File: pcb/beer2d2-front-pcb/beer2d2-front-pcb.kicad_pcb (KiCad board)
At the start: 2 copper layers, 67.9 x 50.8 mm, 177 parts, among them IC1 ATMEGA168P, IC2 5VREG, IC3 TLC5971, J1 PSI_FRONT, J2 EYE_FRONT, J3 PSI_BACK, J4 RGB_EXTRA, J5 DCIN, M3 VAL**, P1 AVR_ISP, Q1 4403, Q10 4401, Q11 4401, Q12 4403, Q13 4401, Q14 4403, Q15 4401, Q2 4403, Q3 4401, Q4 4401, Q5 4403, Q6 4403, Q7 4401, Q8 4401, Q9 4403

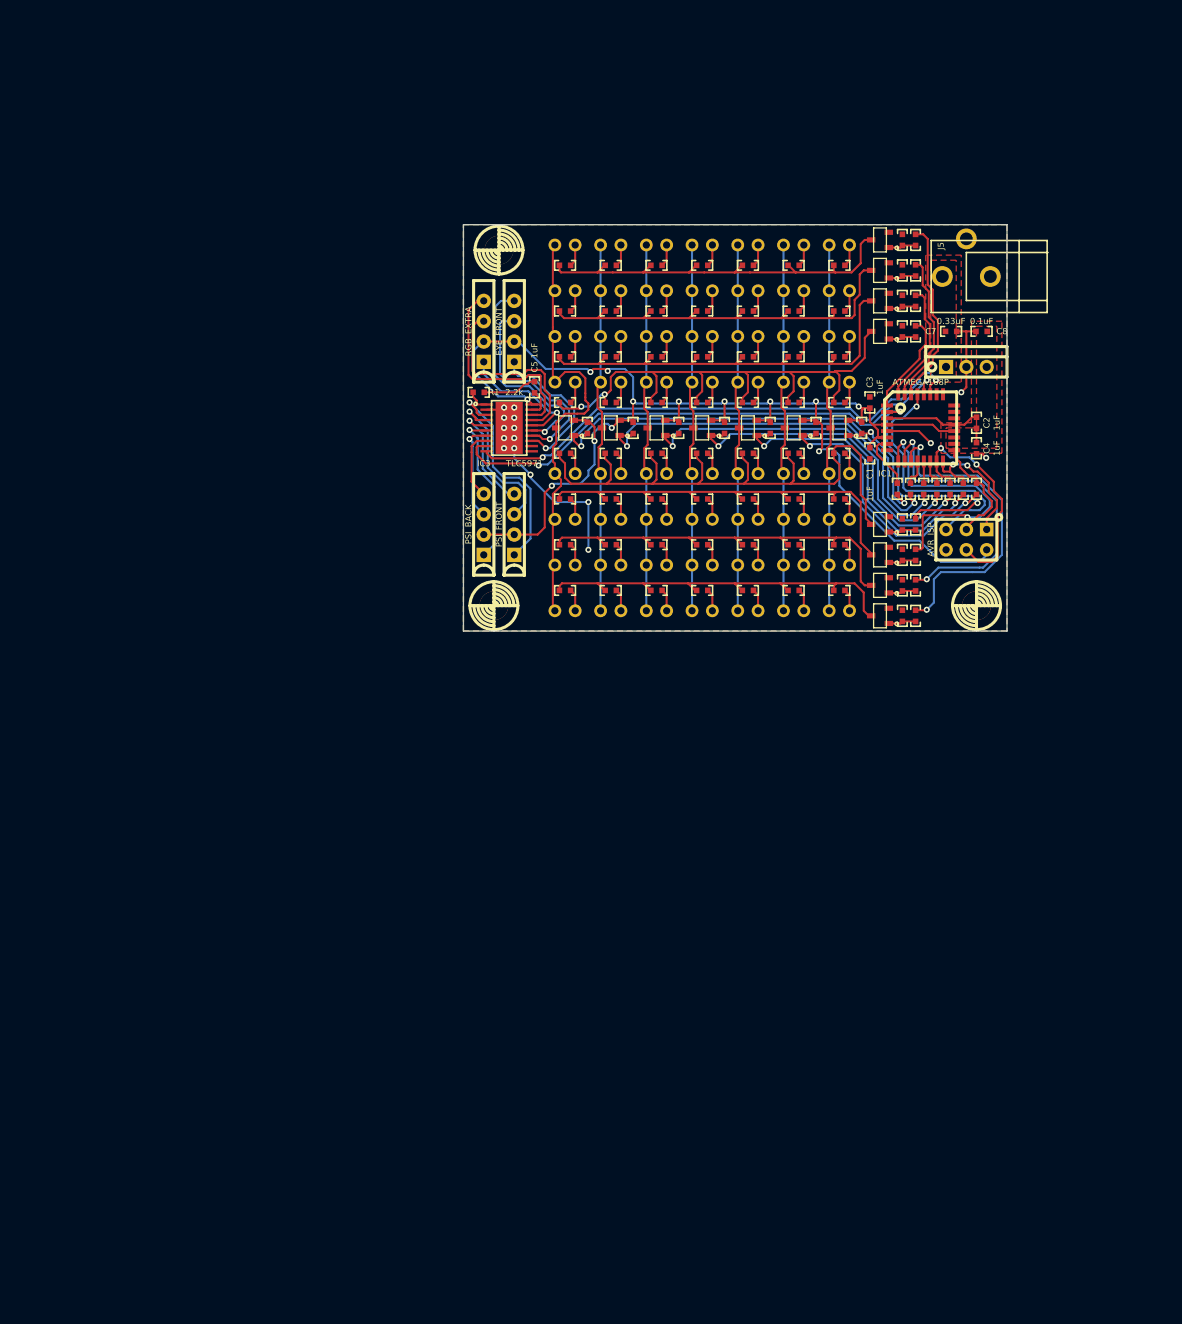
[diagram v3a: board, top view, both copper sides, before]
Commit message: redoing front board
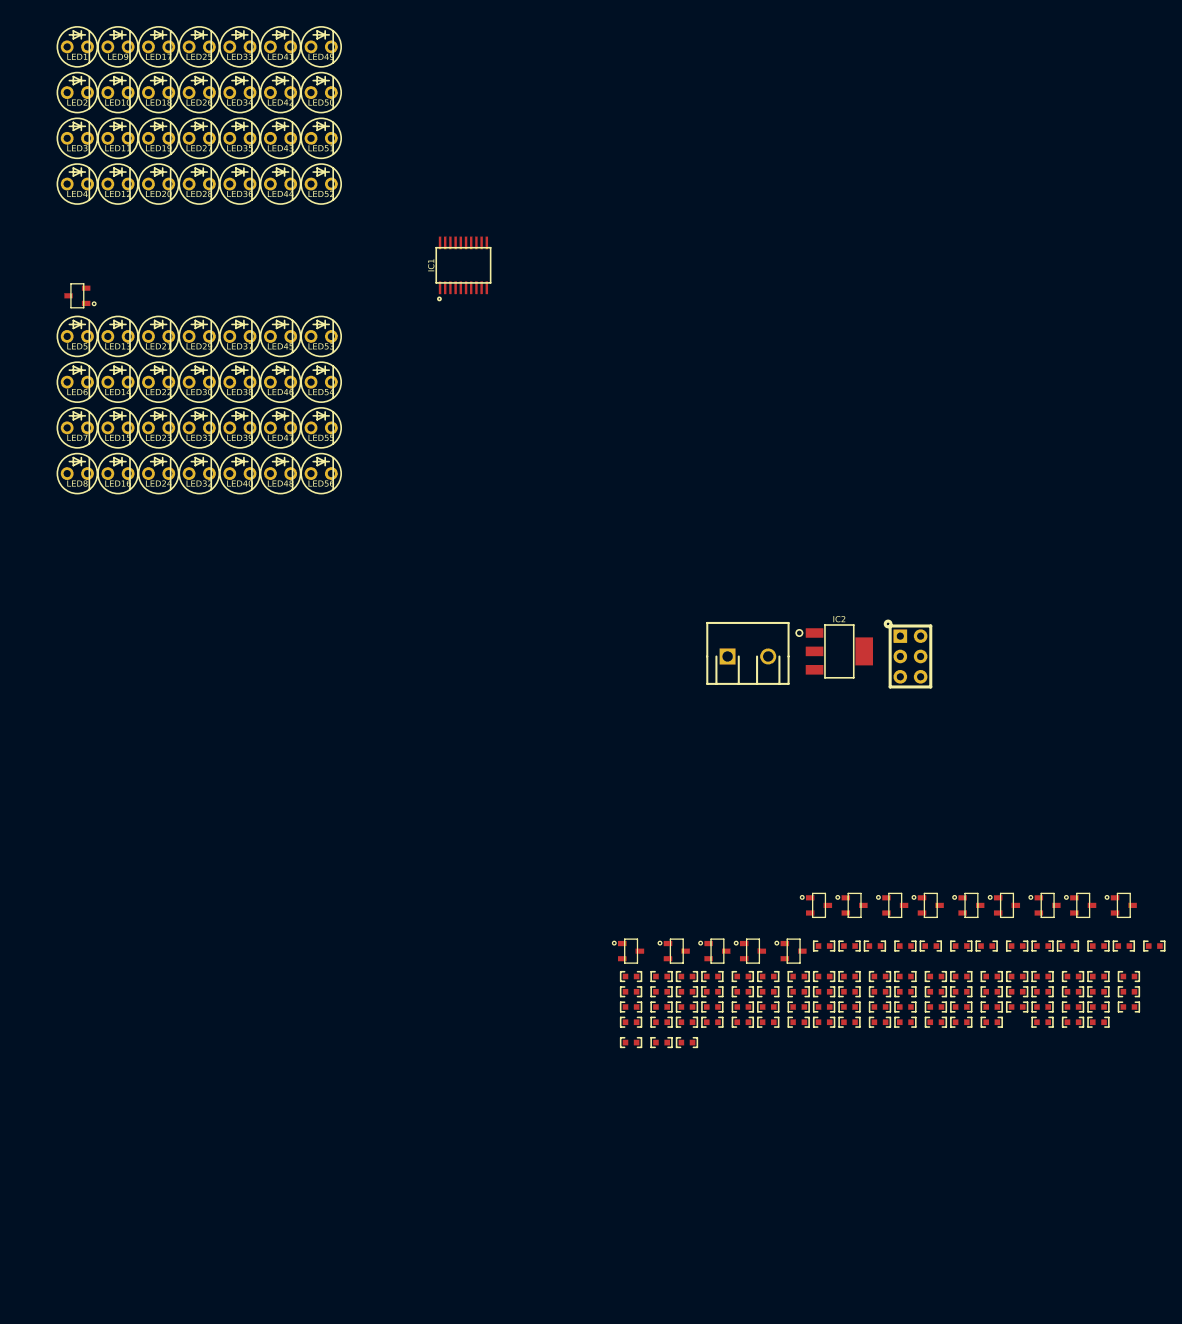
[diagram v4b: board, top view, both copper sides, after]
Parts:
- removed C3, C4: 1uF, 0603(1608m)
- removed C7: 0.1uF, 0603(1608m)
- removed C8: 0.33uF, 0603(1608m)
- removed IC3: TLC5971, HTSSOP20
- removed J2: EYE_FRONT, SIP4
- removed J3: PSI_BACK, SIP4
- removed J4: RGB_EXTRA, SIP4
- removed J5: DCIN, CUI_PJ-102A_DC-BARREL-JACK
- removed M3 (x3): VAL**, M3
- removed R87: 68Ω, 0603(1608m)
- added C6: 0.33uF, 0603(1608m), F.Cu at (233.7, 203.2)
- C1, C2, C5: value 1uF -> 0.1uF
- IC1: value ATMEGA168P -> ATTINY87/167_SO; footprint TQFP32_7mm -> TSSOP20
- IC2: value 5VREG -> LM1117; footprint TO220_3pin -> SOT223
- J1: value PSI_FRONT -> DCIN; footprint SIP4 -> 2-PIN_SCREW-TERM_P200MIL
- LED1, LED10, LED11, LED12, LED13, LED14, LED15, LED16, LED17, LED18, LED19, LED2, LED20, LED21, LED22, LED23, LED24, LED25, LED26, LED27, LED28, LED29, LED3, LED30, LED31, LED32, LED33, LED34, LED35, LED36, LED37, LED38, LED39, LED4, LED40, LED41, LED42, LED43, LED44, LED45, LED46, LED47, LED48, LED49, LED5, LED50, LED51, LED52, LED53, LED54, LED55, LED56, LED6, LED7, LED8, LED9: moved to F.Cu
- R1: value 2.2k -> 68Ω
- R11, R27, R42, R76: value 10kΩ -> 1kΩ
- R15, R31, R66, R78: value 1kΩ -> 10kΩ
- R17, R33, R56, R67, R79: value 10kΩ -> 68Ω
- R25, R41, R53, R75, R9: value 68Ω -> 10kΩ
- R45: value 1kΩ -> 68Ω
- R64: value 68Ω -> 1kΩ
- moved R18 102.5 mm to (261.0, 193.7), turned to 0 degrees
- moved R46 101.8 mm to (264.8, 197.5), turned to 0 degrees
- moved R16 97.1 mm to (264.8, 199.4), turned to 0 degrees
- moved R12 95.3 mm to (257.8, 199.4), turned to 0 degrees
- moved R32 95.1 mm to (210.2, 199.4), turned to 0 degrees
- moved R68 95.0 mm to (247.7, 201.3), turned to 0 degrees
- moved R80 94.8 mm to (237.5, 203.2), turned to 0 degrees
- moved R58 94.3 mm to (261.6, 199.4), turned to 0 degrees
- moved R19 94.2 mm to (254.6, 193.7), turned to 0 degrees
- moved R81 94.2 mm to (268.6, 201.3), turned to 0 degrees
- moved R57 93.2 mm to (230.5, 201.3), turned to 0 degrees
- moved R59 92.6 mm to (268.6, 199.4), turned to 0 degrees
- moved R3 91.6 mm to (243.8, 193.7), turned to 0 degrees
- moved R5 90.4 mm to (257.8, 193.7), turned to 0 degrees
- moved R28 90.2 mm to (244.5, 199.4), turned to 0 degrees
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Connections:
- C5 pad 1: GND -> N-000001
- C5 pad 2: VCC -> GND
- IC1 pad 1: /beer2d2 front LED panel/AVR_R3 -> /beer2d2 front LED panel/AVR_R0
- IC1 pad 10: /beer2d2 front LED panel/AVR_R6 -> /beer2d2 front LED panel/AVR_R7
- IC1 pad 11: /beer2d2 front LED panel/AVR_R7 -> /AVR_RST
- IC1 pad 12: /beer2d2 front LED panel/AVR_C0 -> /beer2d2 front LED panel/AVR_C6
- IC1 pad 13: /beer2d2 front LED panel/AVR_C1 -> /beer2d2 front LED panel/AVR_C5
- IC1 pad 14: /beer2d2 front LED panel/AVR_C2 -> /beer2d2 front LED panel/AVR_C4
- IC1 pad 15: /beer2d2 front LED panel/AVR_C3 -> VCC
- IC1 pad 16: /beer2d2 front LED panel/AVR_C4 -> GND
- IC1 pad 17: /beer2d2 front LED panel/AVR_C5 -> /beer2d2 front LED panel/AVR_C3
- IC1 pad 18: VCC -> /beer2d2 front LED panel/AVR_C2
- IC1 pad 19: (no net) -> /beer2d2 front LED panel/AVR_C1
- IC1 pad 2: /beer2d2 front LED panel/AVR_R4 -> /beer2d2 front LED panel/AVR_R1
- IC1 pad 20: VCC -> /beer2d2 front LED panel/AVR_C0
- IC1 pad 3: GND -> /beer2d2 front LED panel/AVR_R2
- IC1 pad 4: VCC -> /beer2d2 front LED panel/AVR_R3
- IC1 pad 5: GND -> VCC
- IC1 pad 6: VCC -> GND
- IC1 pad 7: /beer2d2 front LED panel/AVR_C6 -> /beer2d2 front LED panel/AVR_R4
- IC1 pad 8: (no net) -> /beer2d2 front LED panel/AVR_R5
- IC1 pad 9: /beer2d2 front LED panel/AVR_R5 -> /beer2d2 front LED panel/AVR_R6
- IC2 pad 1: /VIN -> GND
- IC2 pad 2: GND -> VCC
- IC2 pad 3: VCC -> N-000001
- J1 pad 1: /RED0 -> N-000001
- J1 pad 2: VCC -> GND
- LED1 pad 1: N-00000118 -> N-0000094
- LED10 pad 1: N-00000121 -> N-0000097
- LED11 pad 1: N-00000122 -> N-0000098
- LED12 pad 1: N-0000069 -> N-0000046
- LED13 pad 1: N-0000070 -> N-0000027
- LED14 pad 1: N-0000071 -> N-0000047
- LED15 pad 1: N-0000065 -> N-0000042
- LED16 pad 1: N-0000066 -> N-0000043
- LED17 pad 1: N-0000067 -> N-0000044
- LED18 pad 1: N-0000075 -> N-0000051
- LED19 pad 1: N-0000076 -> N-0000052
- LED2 pad 1: N-00000119 -> N-0000095
- LED20 pad 1: N-0000073 -> N-0000049
- LED21 pad 1: N-0000072 -> N-0000048
- LED22 pad 1: N-0000074 -> N-0000050
- LED23 pad 1: N-0000051 -> N-0000028
- LED24 pad 1: N-0000052 -> N-0000029
- LED25 pad 1: N-0000054 -> N-0000031
- LED26 pad 1: N-0000046 -> N-0000022
- LED27 pad 1: N-0000044 -> N-0000020
- LED28 pad 1: N-0000048 -> N-0000024
- LED29 pad 1: N-0000059 -> N-0000036
- LED3 pad 1: N-00000114 -> N-0000090
- LED30 pad 1: N-0000062 -> N-0000039
- LED31 pad 1: N-0000064 -> N-0000041
- LED32 pad 1: N-0000056 -> N-0000033
- LED33 pad 1: N-0000057 -> N-0000034
- LED34 pad 1: N-0000058 -> N-0000035
- LED35 pad 1: N-0000094 -> N-0000070
- LED36 pad 1: N-0000095 -> N-0000071
- LED37 pad 1: N-0000090 -> N-0000066
- LED38 pad 1: N-0000091 -> N-0000067
- LED39 pad 1: N-0000092 -> N-0000068
- LED4 pad 1: N-00000115 -> N-0000091
- LED40 pad 1: N-0000093 -> N-0000069
- LED41 pad 1: N-0000099 -> N-0000075
- LED42 pad 1: N-00000100 -> N-0000076
- LED43 pad 1: N-0000097 -> N-0000073
- LED44 pad 1: N-0000098 -> N-0000074
- LED45 pad 1: N-0000087 -> N-0000063
- LED46 pad 1: N-0000080 -> N-0000056
- LED47 pad 1: N-0000081 -> N-0000057
- LED48 pad 1: N-0000082 -> N-0000058
- LED49 pad 1: N-0000077 -> N-0000053
- LED5 pad 1: N-00000116 -> N-0000092
- LED50 pad 1: N-0000078 -> N-0000054
- LED51 pad 1: N-0000079 -> N-0000055
- LED52 pad 1: N-0000086 -> N-0000062
- LED53 pad 1: N-0000088 -> N-0000064
- LED54 pad 1: N-0000084 -> N-0000060
- LED55 pad 1: N-0000083 -> N-0000059
- LED56 pad 1: N-0000085 -> N-0000061
- LED6 pad 1: N-00000117 -> N-0000093
- LED7 pad 1: N-00000123 -> N-0000099
- LED8 pad 1: N-00000124 -> N-00000100
- LED9 pad 1: N-00000120 -> N-0000096
- P1 pad 1: /beer2d2 front LED panel/AVR_C4 -> /beer2d2 front LED panel/AVR_R2
- P1 pad 3: /beer2d2 front LED panel/AVR_C5 -> /beer2d2 front LED panel/AVR_R5
- P1 pad 4: /beer2d2 front LED panel/AVR_C3 -> /beer2d2 front LED panel/AVR_R4
- Q1 pad 1: N-00000109 -> N-0000085
- Q10 pad 1: N-00000113 -> N-0000089
- Q11 pad 1: N-00000106 -> N-0000082
- Q12 pad 1: N-00000125 -> N-00000101
- Q13 pad 1: N-00000110 -> N-0000086
- Q14 pad 1: N-00000129 -> N-00000105
- Q15 pad 1: N-00000103 -> N-0000079
- Q2 pad 1: N-00000127 -> N-00000103
- Q3 pad 1: N-00000107 -> N-0000083
- Q4 pad 1: N-00000102 -> N-0000078
- Q5 pad 1: N-00000104 -> N-0000080
- Q6 pad 1: N-00000128 -> N-00000104
- Q7 pad 1: N-00000111 -> N-0000087
- Q8 pad 1: N-00000105 -> N-0000081
- Q9 pad 1: N-00000126 -> N-00000102
- R1 pad 1: GND -> N-0000094
- R1 pad 2: N-0000038 -> /beer2d2 front LED panel/ROW0
- R10 pad 2: N-00000109 -> N-00000103
- R11 pad 1: VCC -> /beer2d2 front LED panel/AVR_R0
- R11 pad 2: N-00000127 -> N-0000083
- R12 pad 1: /beer2d2 front LED panel/AVR_R0 -> /beer2d2 front LED panel/AVR_R5
- R12 pad 2: N-00000107 -> N-0000078
- R13 pad 1: /beer2d2 front LED panel/AVR_R5 -> N-0000085
- R13 pad 2: N-00000102 -> /beer2d2 front LED panel/AVR_C0
- R14 pad 1: N-00000109 -> N-00000103
- R14 pad 2: /beer2d2 front LED panel/AVR_C0 -> /beer2d2 front LED panel/AVR_C5
- R15 pad 1: N-00000127 -> N-0000083
- R15 pad 2: /beer2d2 front LED panel/AVR_C5 -> GND
- R16 pad 1: N-00000107 -> N-0000078
- R17 pad 1: N-00000102 -> N-0000096
- R17 pad 2: GND -> /beer2d2 front LED panel/ROW0
- R18 pad 1: N-00000120 -> N-0000097
- R18 pad 2: /beer2d2 front LED panel/ROW0 -> /beer2d2 front LED panel/ROW1
- R19 pad 1: N-00000121 -> N-0000098
- R19 pad 2: /beer2d2 front LED panel/ROW1 -> /beer2d2 front LED panel/ROW2
- R2 pad 1: N-00000118 -> N-0000095
- R2 pad 2: /beer2d2 front LED panel/ROW0 -> /beer2d2 front LED panel/ROW1
- R20 pad 1: N-00000122 -> N-0000046
- R20 pad 2: /beer2d2 front LED panel/ROW2 -> /beer2d2 front LED panel/ROW3
- R21 pad 1: N-0000069 -> N-0000027
- R21 pad 2: /beer2d2 front LED panel/ROW3 -> /beer2d2 front LED panel/ROW4
- R22 pad 1: N-0000070 -> N-0000047
- R22 pad 2: /beer2d2 front LED panel/ROW4 -> /beer2d2 front LED panel/ROW5
- R23 pad 1: N-0000071 -> N-0000042
- R23 pad 2: /beer2d2 front LED panel/ROW5 -> /beer2d2 front LED panel/ROW6
- R24 pad 1: N-0000065 -> N-0000043
- R24 pad 2: /beer2d2 front LED panel/ROW6 -> /beer2d2 front LED panel/ROW7
- R25 pad 1: N-0000066 -> VCC
- R25 pad 2: /beer2d2 front LED panel/ROW7 -> N-0000080
- R27 pad 1: VCC -> /beer2d2 front LED panel/AVR_R1
- R27 pad 2: N-00000128 -> N-0000087
- R28 pad 1: /beer2d2 front LED panel/AVR_R1 -> /beer2d2 front LED panel/AVR_R6
- R28 pad 2: N-00000111 -> N-0000081
- R29 pad 1: /beer2d2 front LED panel/AVR_R6 -> N-0000080
- R29 pad 2: N-00000105 -> /beer2d2 front LED panel/AVR_C1
- R3 pad 1: N-00000119 -> N-0000090
- R3 pad 2: /beer2d2 front LED panel/ROW1 -> /beer2d2 front LED panel/ROW2
- R30 pad 2: /beer2d2 front LED panel/AVR_C1 -> /beer2d2 front LED panel/AVR_C6
- R31 pad 1: N-00000128 -> N-0000087
- R31 pad 2: /beer2d2 front LED panel/AVR_C6 -> GND
- R32 pad 1: N-00000111 -> N-0000081
- R33 pad 1: N-00000105 -> N-0000044
- R33 pad 2: GND -> /beer2d2 front LED panel/ROW0
- R34 pad 1: N-0000067 -> N-0000051
- R34 pad 2: /beer2d2 front LED panel/ROW0 -> /beer2d2 front LED panel/ROW1
- R35 pad 1: N-0000075 -> N-0000052
- R35 pad 2: /beer2d2 front LED panel/ROW1 -> /beer2d2 front LED panel/ROW2
- R36 pad 1: N-0000076 -> N-0000049
- R36 pad 2: /beer2d2 front LED panel/ROW2 -> /beer2d2 front LED panel/ROW3
- R37 pad 1: N-0000073 -> N-0000048
- R37 pad 2: /beer2d2 front LED panel/ROW3 -> /beer2d2 front LED panel/ROW4
- R38 pad 1: N-0000072 -> N-0000050
- R38 pad 2: /beer2d2 front LED panel/ROW4 -> /beer2d2 front LED panel/ROW5
- R39 pad 1: N-0000074 -> N-0000028
- R39 pad 2: /beer2d2 front LED panel/ROW5 -> /beer2d2 front LED panel/ROW6
- R4 pad 1: N-00000114 -> N-0000091
- R4 pad 2: /beer2d2 front LED panel/ROW2 -> /beer2d2 front LED panel/ROW3
- R40 pad 1: N-0000051 -> N-0000029
- R40 pad 2: /beer2d2 front LED panel/ROW6 -> /beer2d2 front LED panel/ROW7
- R41 pad 1: N-0000052 -> VCC
- R41 pad 2: /beer2d2 front LED panel/ROW7 -> N-00000102
- R42 pad 1: VCC -> /beer2d2 front LED panel/AVR_R2
- R42 pad 2: N-00000126 -> N-0000089
- R43 pad 1: /beer2d2 front LED panel/AVR_R2 -> /beer2d2 front LED panel/AVR_R7
- R43 pad 2: N-00000113 -> N-0000082
- R44 pad 1: /beer2d2 front LED panel/AVR_R7 -> N-00000102
- R44 pad 2: N-00000106 -> /beer2d2 front LED panel/AVR_C2
- R45 pad 1: N-00000126 -> N-0000031
- R45 pad 2: /beer2d2 front LED panel/AVR_C2 -> /beer2d2 front LED panel/ROW0
- R46 pad 1: N-0000054 -> N-0000022
- R46 pad 2: /beer2d2 front LED panel/ROW0 -> /beer2d2 front LED panel/ROW1
- R47 pad 1: N-0000046 -> N-0000020
- R47 pad 2: /beer2d2 front LED panel/ROW1 -> /beer2d2 front LED panel/ROW2
- R48 pad 1: N-0000044 -> N-0000024
- R48 pad 2: /beer2d2 front LED panel/ROW2 -> /beer2d2 front LED panel/ROW3
- R49 pad 1: N-0000048 -> N-0000036
- R49 pad 2: /beer2d2 front LED panel/ROW3 -> /beer2d2 front LED panel/ROW4
- R5 pad 1: N-00000115 -> N-0000092
- R5 pad 2: /beer2d2 front LED panel/ROW3 -> /beer2d2 front LED panel/ROW4
- R50 pad 1: N-0000059 -> N-0000039
- R50 pad 2: /beer2d2 front LED panel/ROW4 -> /beer2d2 front LED panel/ROW5
- R51 pad 1: N-0000062 -> N-0000041
- R51 pad 2: /beer2d2 front LED panel/ROW5 -> /beer2d2 front LED panel/ROW6
- R52 pad 1: N-0000064 -> N-0000033
- R52 pad 2: /beer2d2 front LED panel/ROW6 -> /beer2d2 front LED panel/ROW7
- R53 pad 1: N-0000056 -> N-0000089
- R53 pad 2: /beer2d2 front LED panel/ROW7 -> GND
- R54 pad 1: N-00000113 -> N-0000082
- R55 pad 1: N-00000106 -> VCC
- R55 pad 2: GND -> N-00000101
- R56 pad 1: VCC -> N-0000034
- R56 pad 2: N-00000125 -> /beer2d2 front LED panel/ROW0
- R57 pad 1: N-0000057 -> N-0000035
- R57 pad 2: /beer2d2 front LED panel/ROW0 -> /beer2d2 front LED panel/ROW1
- R58 pad 1: N-0000058 -> N-0000070
- R58 pad 2: /beer2d2 front LED panel/ROW1 -> /beer2d2 front LED panel/ROW2
- R59 pad 1: N-0000094 -> N-0000071
- R59 pad 2: /beer2d2 front LED panel/ROW2 -> /beer2d2 front LED panel/ROW3
- R6 pad 1: N-00000116 -> N-0000093
- R6 pad 2: /beer2d2 front LED panel/ROW4 -> /beer2d2 front LED panel/ROW5
- R60 pad 1: N-0000095 -> N-0000066
- R60 pad 2: /beer2d2 front LED panel/ROW3 -> /beer2d2 front LED panel/ROW4
- R61 pad 1: N-0000090 -> N-0000067
- R61 pad 2: /beer2d2 front LED panel/ROW4 -> /beer2d2 front LED panel/ROW5
- R62 pad 1: N-0000091 -> N-0000068
- R62 pad 2: /beer2d2 front LED panel/ROW5 -> /beer2d2 front LED panel/ROW6
- R63 pad 1: N-0000092 -> N-0000069
- R63 pad 2: /beer2d2 front LED panel/ROW6 -> /beer2d2 front LED panel/ROW7
- R64 pad 1: N-0000093 -> /beer2d2 front LED panel/AVR_R3
- R64 pad 2: /beer2d2 front LED panel/ROW7 -> N-0000086
- R65 pad 1: /beer2d2 front LED panel/AVR_R3 -> N-00000101
- R65 pad 2: N-00000110 -> /beer2d2 front LED panel/AVR_C3
- R66 pad 1: N-00000125 -> N-0000086
- R66 pad 2: /beer2d2 front LED panel/AVR_C3 -> GND
- R67 pad 1: N-00000110 -> N-0000075
- R67 pad 2: GND -> /beer2d2 front LED panel/ROW0
- R68 pad 1: N-0000099 -> N-0000076
- R68 pad 2: /beer2d2 front LED panel/ROW0 -> /beer2d2 front LED panel/ROW1
- R69 pad 1: N-00000100 -> N-0000073
- R69 pad 2: /beer2d2 front LED panel/ROW1 -> /beer2d2 front LED panel/ROW2
- R7 pad 1: N-00000117 -> N-0000099
- R7 pad 2: /beer2d2 front LED panel/ROW5 -> /beer2d2 front LED panel/ROW6
- R70 pad 1: N-0000097 -> N-0000074
- R70 pad 2: /beer2d2 front LED panel/ROW2 -> /beer2d2 front LED panel/ROW3
- R71 pad 1: N-0000098 -> N-0000063
- R71 pad 2: /beer2d2 front LED panel/ROW3 -> /beer2d2 front LED panel/ROW4
- R72 pad 1: N-0000087 -> N-0000056
- R72 pad 2: /beer2d2 front LED panel/ROW4 -> /beer2d2 front LED panel/ROW5
- R73 pad 1: N-0000080 -> N-0000057
- R73 pad 2: /beer2d2 front LED panel/ROW5 -> /beer2d2 front LED panel/ROW6
- R74 pad 1: N-0000081 -> N-0000058
- R74 pad 2: /beer2d2 front LED panel/ROW6 -> /beer2d2 front LED panel/ROW7
- R75 pad 1: N-0000082 -> VCC
- R75 pad 2: /beer2d2 front LED panel/ROW7 -> N-00000105
- R76 pad 1: VCC -> /beer2d2 front LED panel/AVR_R4
- R76 pad 2: N-00000129 -> N-0000079
- R77 pad 1: /beer2d2 front LED panel/AVR_R4 -> N-00000105
- R77 pad 2: N-00000103 -> /beer2d2 front LED panel/AVR_C4
- R78 pad 1: N-00000129 -> N-0000079
- R78 pad 2: /beer2d2 front LED panel/AVR_C4 -> GND
- R79 pad 1: N-00000103 -> N-0000053
- R79 pad 2: GND -> /beer2d2 front LED panel/ROW0
- R8 pad 1: N-00000123 -> N-00000100
- R8 pad 2: /beer2d2 front LED panel/ROW6 -> /beer2d2 front LED panel/ROW7
- R80 pad 1: N-0000077 -> N-0000054
- R80 pad 2: /beer2d2 front LED panel/ROW0 -> /beer2d2 front LED panel/ROW1
- R81 pad 1: N-0000078 -> N-0000055
- R81 pad 2: /beer2d2 front LED panel/ROW1 -> /beer2d2 front LED panel/ROW2
- R82 pad 1: N-0000079 -> N-0000062
- R82 pad 2: /beer2d2 front LED panel/ROW2 -> /beer2d2 front LED panel/ROW3
- R83 pad 1: N-0000086 -> N-0000064
- R83 pad 2: /beer2d2 front LED panel/ROW3 -> /beer2d2 front LED panel/ROW4
- R84 pad 1: N-0000088 -> N-0000060
- R84 pad 2: /beer2d2 front LED panel/ROW4 -> /beer2d2 front LED panel/ROW5
- R85 pad 1: N-0000084 -> N-0000059
- R85 pad 2: /beer2d2 front LED panel/ROW5 -> /beer2d2 front LED panel/ROW6
- R86 pad 1: N-0000083 -> N-0000061
- R86 pad 2: /beer2d2 front LED panel/ROW6 -> /beer2d2 front LED panel/ROW7
- R9 pad 1: N-00000124 -> VCC
- R9 pad 2: /beer2d2 front LED panel/ROW7 -> N-0000085
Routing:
- net VCC: track 187.4 -> 0.00 mm, vias 13 -> 0
- net /beer2d2 front LED panel/ROW4: track 76.9 -> 0.00 mm
- net GND: track 74.1 -> 0.00 mm, vias 16 -> 0
- net /beer2d2 front LED panel/ROW3: track 68.8 -> 0.00 mm, vias 2 -> 0
- net /TLC_SDA: track 66.5 -> 0.00 mm, vias 2 -> 0
- net /TLC_SCK: track 65.0 -> 0.00 mm, vias 2 -> 0
- net N-00000109: track 56.6 -> 0.00 mm, vias 2 -> 0
- net /beer2d2 front LED panel/COL0: track 56.3 -> 0.00 mm
- net /beer2d2 front LED panel/ROW2: track 53.7 -> 0.00 mm
- net /beer2d2 front LED panel/ROW5: track 53.7 -> 0.00 mm
- net N-00000104: track 52.2 -> 0.00 mm, vias 2 -> 0
- net /beer2d2 front LED panel/ROW6: track 52.1 -> 0.00 mm
- net /beer2d2 front LED panel/ROW1: track 52.0 -> 0.00 mm
- net /beer2d2 front LED panel/ROW7: track 50.4 -> 0.00 mm
- net /beer2d2 front LED panel/ROW0: track 50.4 -> 0.00 mm
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- removed copper zone on F.Cu, net /VIN
- removed copper zone on B.Cu, net GND
- removed copper zone on F.Cu, net GND
- removed copper zone on F.Cu, net VCC
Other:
- board outline removed

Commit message: layout complete
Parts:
- removed R10, R15, R16, R25, R26, R31, R32, R41, R53, R54, R55, R66, R75, R78, R9: 10kΩ, 0603(1608m)
- removed R11, R12, R13, R14, R27, R28, R29, R30, R42, R43, R44, R64, R65, R76, R77: 1kΩ, 0603(1608m)
- added M3: VAL**, M3, F.Cu at (174.0, 134.0)
- added M3: VAL**, M3, F.Cu at (174.0, 81.9)
- IC1: value ATTINY87/167_SO -> ATTINY167
- J1: value DCIN -> 6-12V
- LED1, LED10, LED11, LED12, LED13, LED14, LED15, LED16, LED17, LED18, LED19, LED2, LED20, LED21, LED22, LED23, LED24, LED25, LED26, LED27, LED28, LED29, LED3, LED30, LED31, LED32, LED33, LED34, LED35, LED36, LED37, LED38, LED39, LED4, LED40, LED41, LED42, LED43, LED44, LED45, LED46, LED47, LED48, LED49, LED5, LED50, LED51, LED52, LED53, LED54, LED55, LED56, LED6, LED7, LED8, LED9: moved to B.Cu
- Q1, Q2, Q5, Q6, Q9: value 4403 -> DDTB113ZC
- Q10, Q13: value 4401 -> DDTB113ZC
- Q11, Q15, Q3, Q4, Q7, Q8: value 4401 -> DDTD113ZC
- Q12, Q14: value 4403 -> DDTD113ZC
- moved R17 168.0 mm to (142.2, 78.7), turned to 180 degrees
- moved R18 161.3 mm to (142.2, 84.5), turned to 180 degrees
- moved R46 159.4 mm to (152.4, 84.5), turned to 180 degrees
- moved R45 158.8 mm to (152.4, 78.7), turned to 180 degrees
- moved R67 153.3 mm to (162.6, 78.7), turned to 180 degrees
- moved R19 152.8 mm to (142.2, 90.2), turned to 180 degrees
- moved R59 151.9 mm to (157.5, 95.9), turned to 180 degrees
- moved R58 150.9 mm to (157.5, 90.2), turned to 180 degrees
- moved R56 150.6 mm to (157.5, 78.7), turned to 180 degrees
- moved R81 150.1 mm to (167.6, 90.2), turned to 180 degrees
- moved C1 149.8 mm to (146.1, 108.0), turned to 90 degrees
- moved Q14 149.3 mm to (137.2, 101.6), turned to 90 degrees
- moved R3 148.6 mm to (137.2, 90.2), turned to 180 degrees
- moved R20 146.1 mm to (142.2, 95.9), turned to 180 degrees
- moved R1 145.9 mm to (137.2, 78.7), turned to 180 degrees
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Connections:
- Q1 pad 1: N-0000085 (its old number) -> /beer2d2 front LED panel/AVR_C0
- Q10 pad 1: N-0000089 (its old number) -> /beer2d2 front LED panel/AVR_C5
- Q10 pad 2: GND -> VCC
- Q10 pad 3: /beer2d2 front LED panel/ROW2 -> /beer2d2 front LED panel/COL5
- Q11 pad 1: N-0000082 (its old number) -> /beer2d2 front LED panel/AVR_R4
- Q11 pad 3: /beer2d2 front LED panel/ROW7 -> /beer2d2 front LED panel/ROW4
- Q12 pad 1: N-00000101 -> /beer2d2 front LED panel/AVR_R5
- Q12 pad 2: VCC -> GND
- Q12 pad 3: /beer2d2 front LED panel/COL3 -> /beer2d2 front LED panel/ROW5
- Q13 pad 1: N-0000086 (its old number) -> /beer2d2 front LED panel/AVR_C6
- Q13 pad 2: GND -> VCC
- Q13 pad 3: /beer2d2 front LED panel/ROW3 -> /beer2d2 front LED panel/COL6
- Q14 pad 1: N-00000105 -> /beer2d2 front LED panel/AVR_R6
- Q14 pad 2: VCC -> GND
- Q14 pad 3: /beer2d2 front LED panel/COL4 -> /beer2d2 front LED panel/ROW6
- Q15 pad 1: N-0000079 (its old number) -> /beer2d2 front LED panel/AVR_R7
- Q15 pad 3: /beer2d2 front LED panel/ROW4 -> /beer2d2 front LED panel/ROW7
- Q2 pad 1: N-00000103 -> /beer2d2 front LED panel/AVR_C1
- Q2 pad 3: /beer2d2 front LED panel/COL5 -> /beer2d2 front LED panel/COL1
- Q3 pad 1: N-0000083 (its old number) -> /beer2d2 front LED panel/AVR_R0
- Q4 pad 1: N-0000078 (its old number) -> /beer2d2 front LED panel/AVR_R1
- Q4 pad 3: /beer2d2 front LED panel/ROW5 -> /beer2d2 front LED panel/ROW1
- Q5 pad 1: N-0000080 (its old number) -> /beer2d2 front LED panel/AVR_C2
- Q5 pad 3: /beer2d2 front LED panel/COL1 -> /beer2d2 front LED panel/COL2
- Q6 pad 1: N-00000104 -> /beer2d2 front LED panel/AVR_C3
- Q6 pad 3: /beer2d2 front LED panel/COL6 -> /beer2d2 front LED panel/COL3
- Q7 pad 1: N-0000087 (its old number) -> /beer2d2 front LED panel/AVR_R2
- Q7 pad 3: /beer2d2 front LED panel/ROW1 -> /beer2d2 front LED panel/ROW2
- Q8 pad 1: N-0000081 (its old number) -> /beer2d2 front LED panel/AVR_R3
- Q8 pad 3: /beer2d2 front LED panel/ROW6 -> /beer2d2 front LED panel/ROW3
- Q9 pad 1: N-00000102 -> /beer2d2 front LED panel/AVR_C4
- Q9 pad 3: /beer2d2 front LED panel/COL2 -> /beer2d2 front LED panel/COL4
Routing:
- net VCC: track 0.00 -> 108.9 mm, vias 0 -> 4
- net /beer2d2 front LED panel/COL0: track 0.00 -> 96.3 mm
- net /beer2d2 front LED panel/ROW7: track 0.00 -> 95.0 mm, vias 0 -> 2
- net /beer2d2 front LED panel/COL1: track 0.00 -> 88.5 mm
- net /beer2d2 front LED panel/ROW0: track 0.00 -> 79.3 mm, vias 0 -> 2
- net /beer2d2 front LED panel/COL2: track 0.00 -> 79.0 mm
- net /beer2d2 front LED panel/ROW6: track 0.00 -> 74.1 mm
- net /beer2d2 front LED panel/ROW5: track 0.00 -> 70.3 mm, vias 0 -> 4
- net /beer2d2 front LED panel/COL3: track 0.00 -> 69.9 mm
- net /beer2d2 front LED panel/COL6: track 0.00 -> 67.1 mm
- net /beer2d2 front LED panel/COL4: track 0.00 -> 63.3 mm
- net /beer2d2 front LED panel/COL5: track 0.00 -> 62.9 mm
- net /beer2d2 front LED panel/ROW4: track 0.00 -> 60.2 mm, vias 0 -> 2
- net /beer2d2 front LED panel/ROW1: track 0.00 -> 56.6 mm, vias 0 -> 2
- net /beer2d2 front LED panel/ROW2: track 0.00 -> 50.9 mm, vias 0 -> 2
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- added copper zone on B.Cu, net GND
- added copper zone on F.Cu, net GND
- added copper zone on F.Cu, net N-000001
- added copper zone on F.Cu, net VCC
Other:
- board outline added: 44.4 x 61 mm
- board text added: "beer2d2 front led panel mjc 01/23/2014 open source hardware github.com/mcous/beer2d2"
